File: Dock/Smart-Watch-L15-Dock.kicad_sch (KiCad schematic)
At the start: 1 part, among them P2 ARM JTAG/SWD

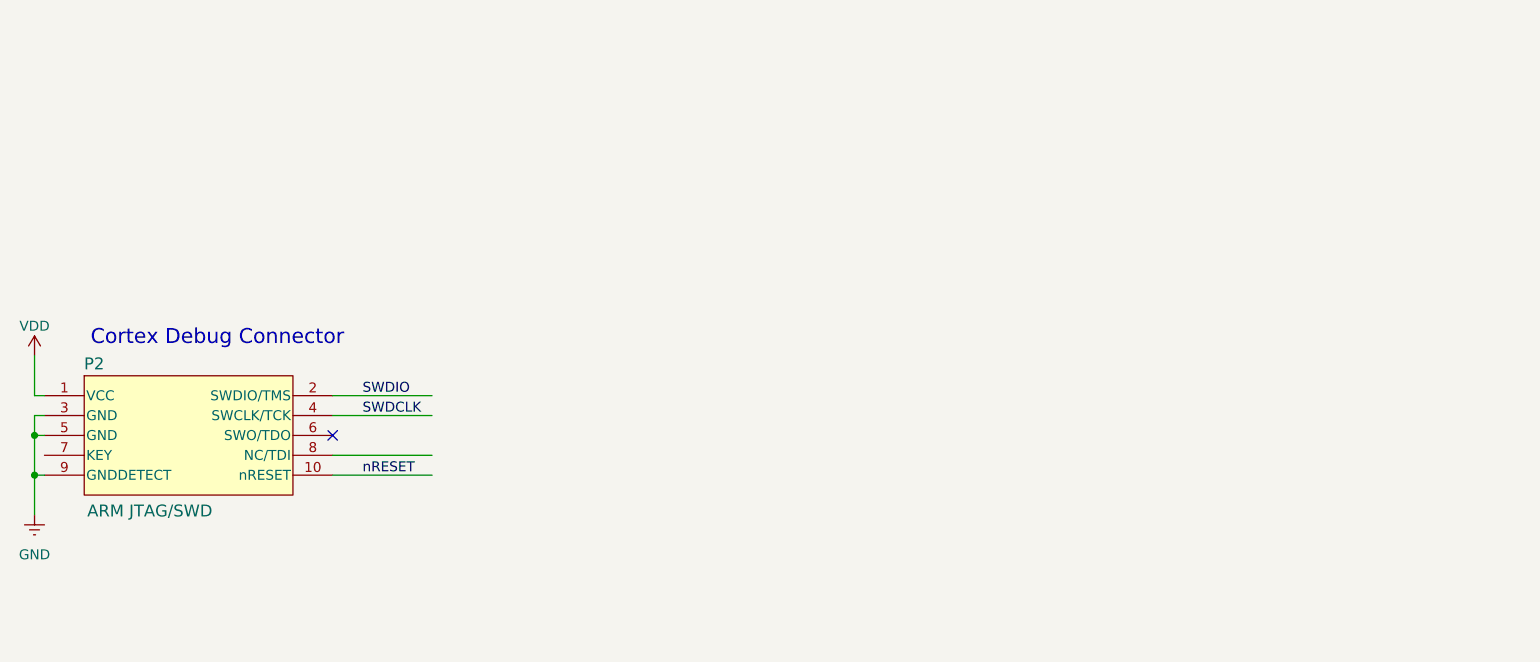
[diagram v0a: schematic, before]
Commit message: Schematic for Dock Done
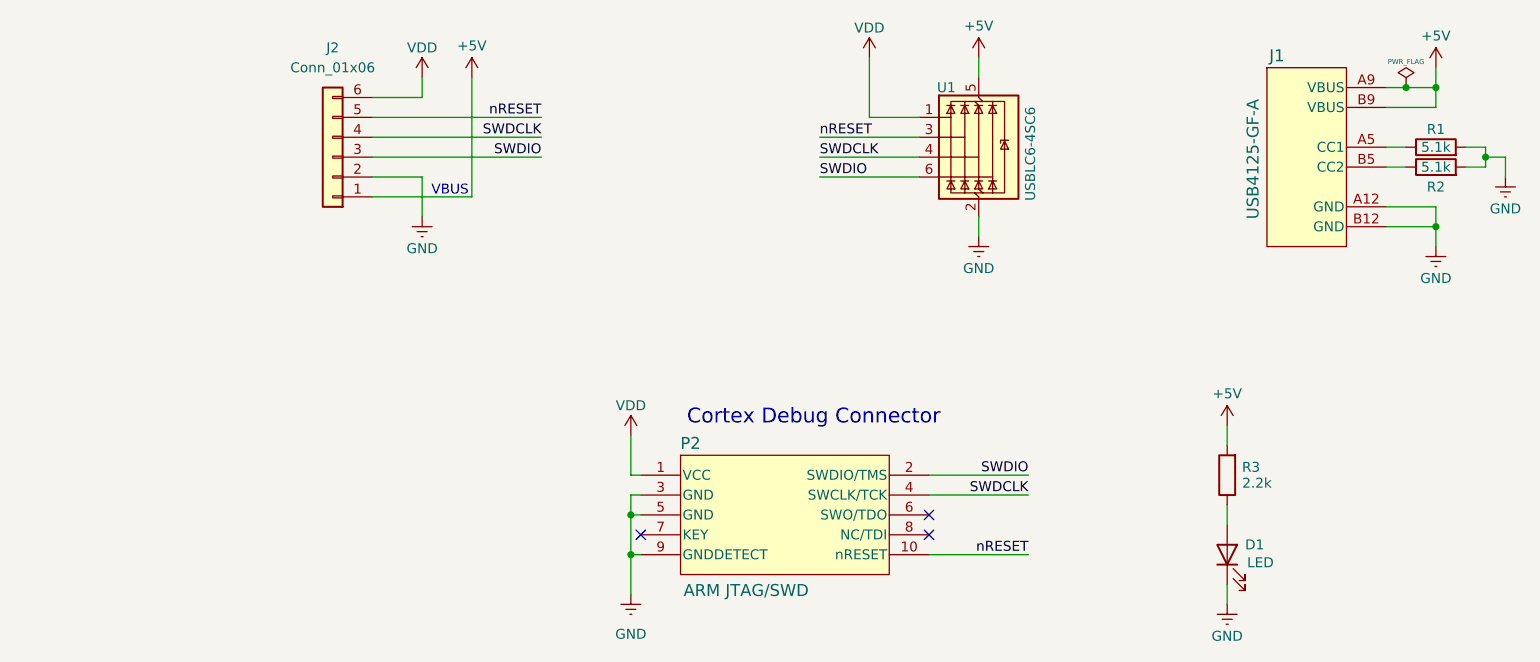
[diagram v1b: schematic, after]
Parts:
- added D1: LED, LED_SMD:LED_0603_1608Metric_Pad1.05x0.95mm_HandSolder, symbol Device:LED
- added J1: USB4125-GF-A, 1_I_Syst.inc:CONN6_USB4125_GCT, symbol 1_I_Syst.inc:USB4125-GF-A
- added J2: Conn_01x06, Connector_PinHeader_2.54mm:PinHeader_1x06_P2.54mm_Vertical, symbol Connector_Generic:Conn_01x06
- added R1, R2: 5.1k, Resistor_SMD:R_0805_2012Metric_Pad1.20x1.40mm_HandSolder, symbol Device:R
- added R3: 2.2k, Resistor_SMD:R_0805_2012Metric_Pad1.20x1.40mm_HandSolder, symbol Device:R
- added U1: USBLC6-4SC6, Package_TO_SOT_SMD:SOT-23-6, symbol Power_Protection:USBLC6-4SC6
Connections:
- net GND: now also D1.1 (K), J1.A12 (GND), J1.B12 (GND), J2.2 (Pin_2), R1.2, R2.2, U1.2 (GND)
- net SWDCLK: now also J2.4 (Pin_4), U1.4 (I/O3)
- net SWDIO: now also J2.3 (Pin_3), U1.6 (I/O4)
- net VDD: now also J2.6 (Pin_6), U1.1 (I/O1)
- net nRESET: now also J2.5 (Pin_5), U1.3 (I/O2)
- new net: D1.2 (A), R3.1
- new net: J1.B5 (CC2), R2.1
- new net: J1.A5 (CC1), R1.1
- new net +5V: J1.A9 (VBUS), J1.B9 (VBUS), J2.1 (Pin_1), R3.2, U1.5 (VBUS)
- no-connect marks 1 -> 3
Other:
- note added: "VBUS"
- company: (none) -> I-Syst.inc
- title: (none) -> Blystwatch Dock
- moved on the sheet: P2
